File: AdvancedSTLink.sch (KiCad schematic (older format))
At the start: 49 parts, among them J1 USB_C_Receptacle, J2 Conn_02x03_Odd_Even, J3 Conn_01x06, J4 Conn_02x03_Odd_Even, SW1 SW_SPDT, U1 STM32F205RETx, U2 XC6206P332MR, U3 USBLC6-2P6, U4 MP2359, U5 USBLC6-2P6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

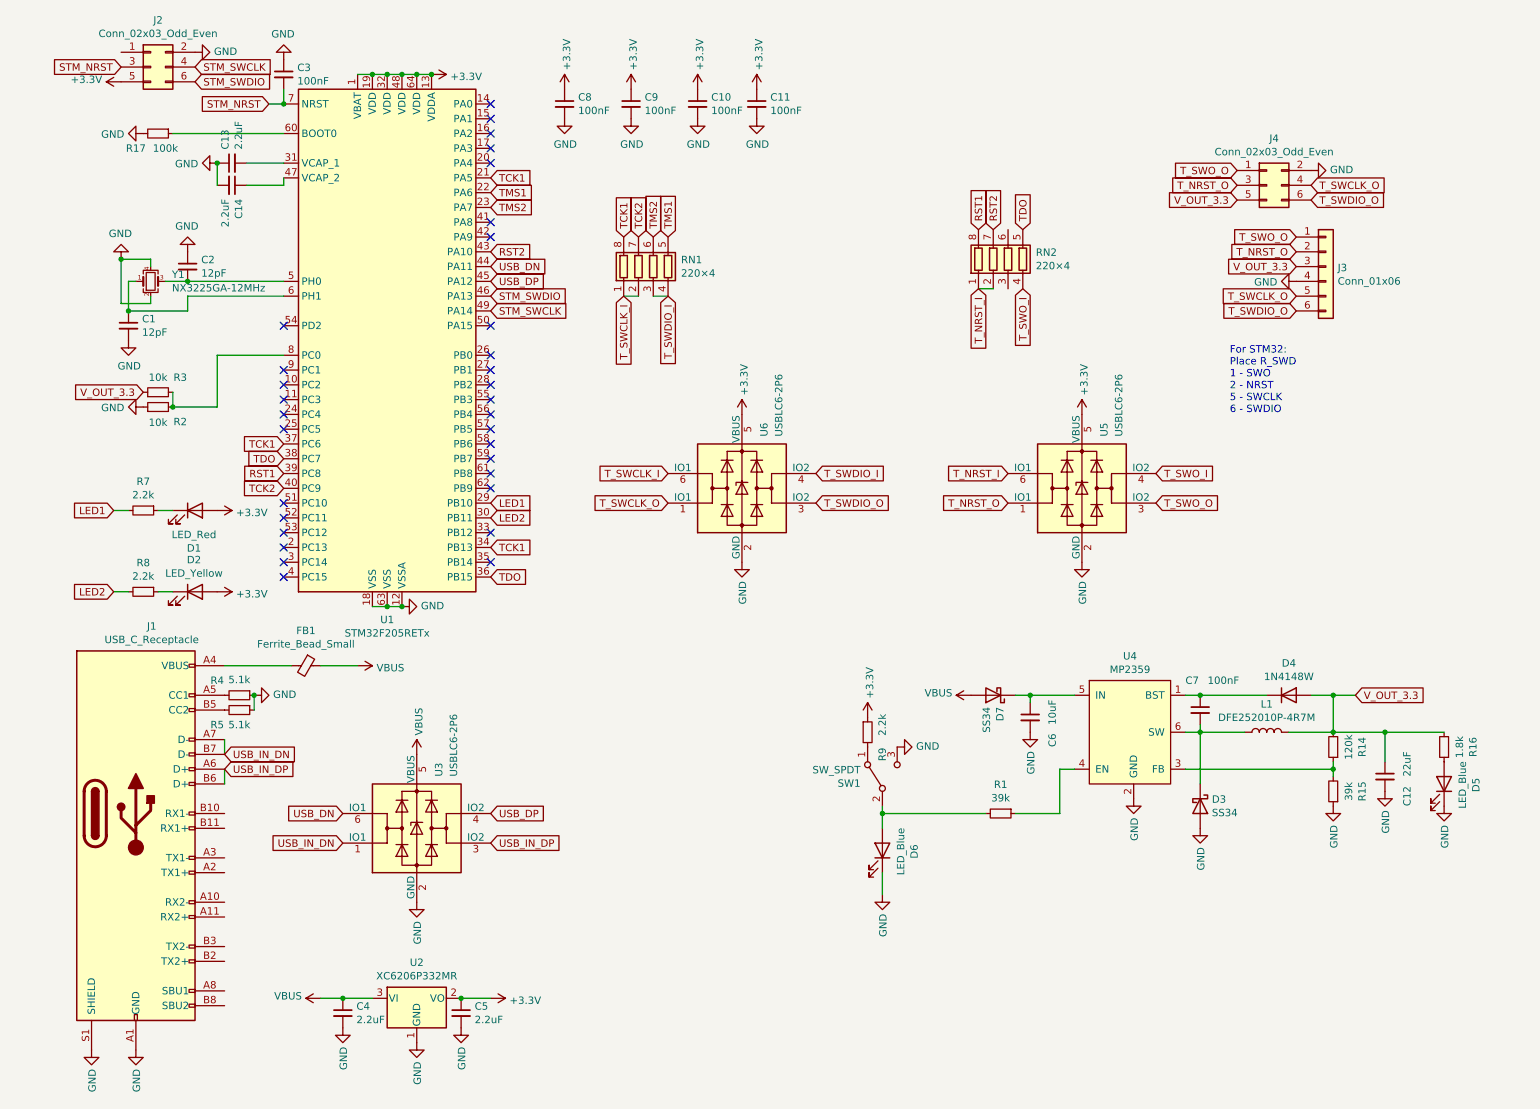
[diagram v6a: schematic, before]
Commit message: Put components.
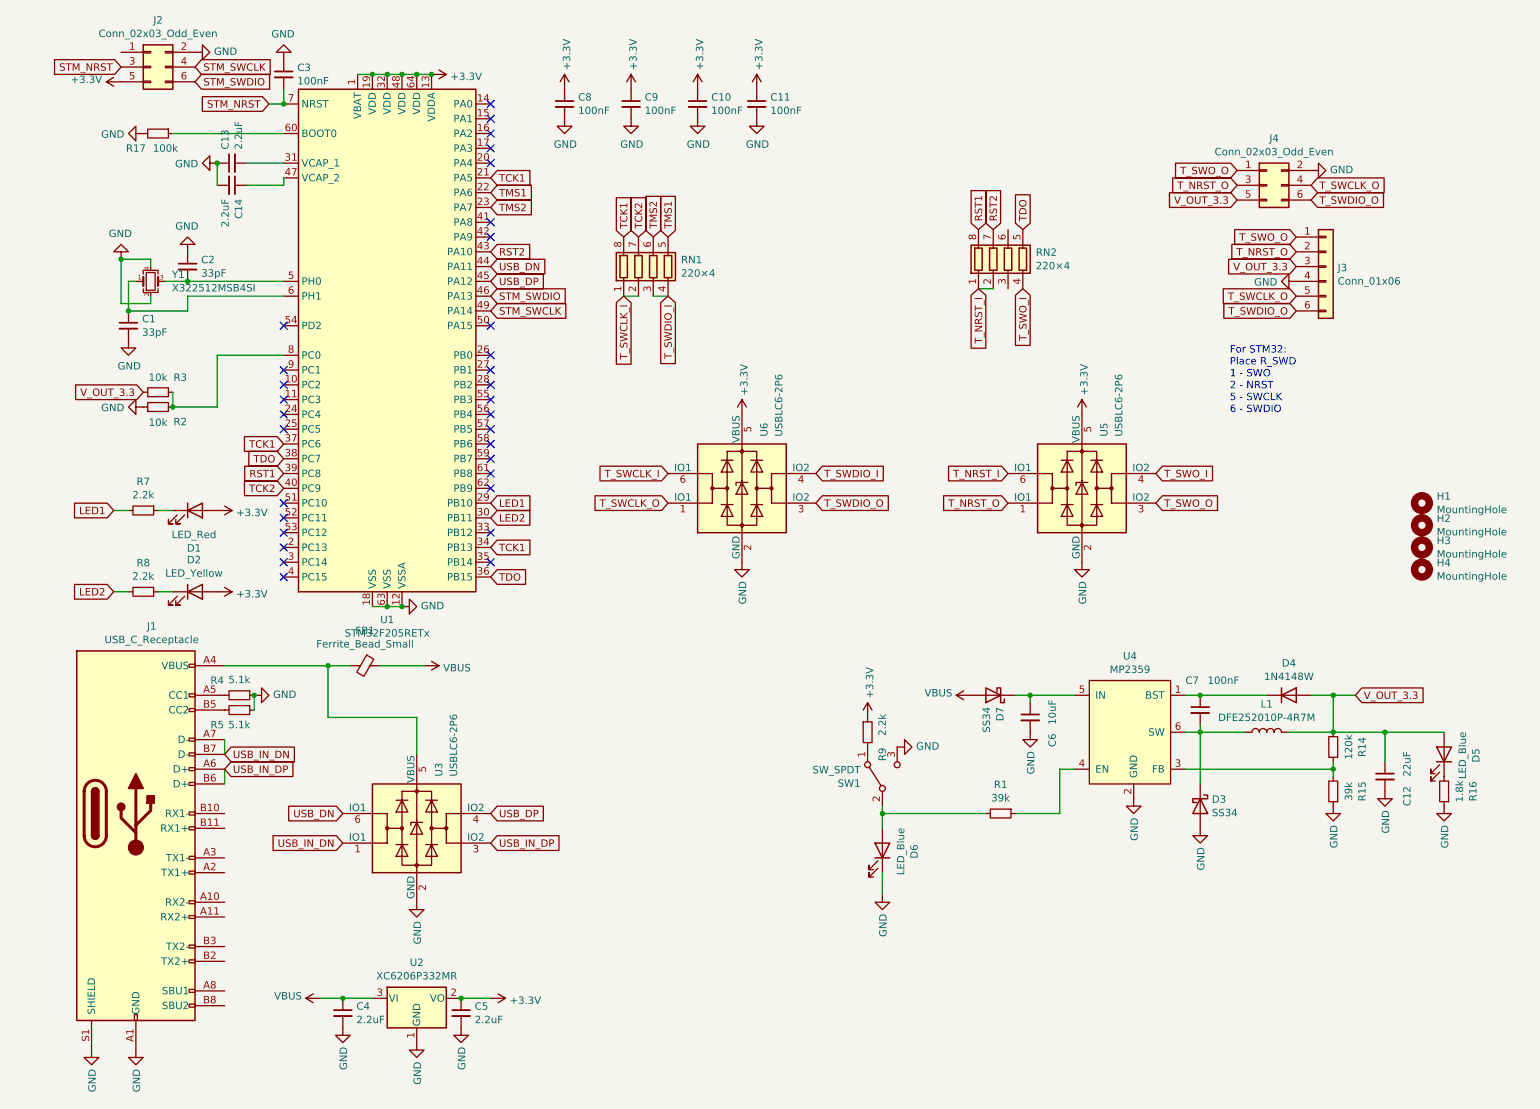
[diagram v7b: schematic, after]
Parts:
- added H1, H2, H3, H4: MountingHole, MountingHole:MountingHole_2.5mm, symbol Mechanical:MountingHole
- C1, C2: value 12pF -> 33pF
- D4: footprint lc:SOD-123 -> lc:SOD-323
- R3: footprint Resistor_SMD:R_0603_1608Metric -> Resistor_SMD:R_0402_1005Metric
- Y1: value NX3225GA-12MHz -> X322512MSB4SI; JLC-ID (none) -> C9002
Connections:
- net GND: now also R16.1; no longer D5.1 (K)
- net VBUS: no longer U3.5 (VBUS)
- net V_OUT_3.3: now also D5.2 (A); no longer R16.2
- net at FB1.2, J1.A4 (VBUS), J1.A9 (VBUS)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: now also U3.5 (VBUS)
- new net: D5.1 (K), R16.2
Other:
- moved on the sheet: D5, FB1, R16
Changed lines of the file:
@@
 P 1050 2600
 F 0 "C1" H 1142 2646 50  0000 L CNN
-F 1 "12pF" H 1142 2555 50  0000 L CNN
+F 1 "33pF" H 1142 2555 50  0000 L CNN
 F 2 "Capacitor_SMD:C_0402_1005Metric" H 1050 2600 50  0001 C CNN
 F 3 "~" H 1050 2600 50  0001 C CNN
@@
 P 1450 2200
 F 0 "C2" H 1542 2246 50  0000 L CNN
-F 1 "12pF" H 1542 2155 50  0000 L CNN
+F 1 "33pF" H 1542 2155 50  0000 L CNN
 F 2 "Capacitor_SMD:C_0402_1005Metric" H 1450 2200 50  0001 C CNN
 F 3 "~" H 1450 2200 50  0001 C CNN
@@
 F 0 "R3" V 1350 2900 50  0000 C CNN
 F 1 "10k" V 1350 3050 50  0000 C CNN
-F 2 "Resistor_SMD:R_0603_1608Metric" H 1250 3050 50  0001 C CNN
+F 2 "Resistor_SMD:R_0402_1005Metric" H 1250 3050 50  0001 C CNN
 F 3 "~" H 1250 3050 50  0001 C CNN
 	1    1250 3050
@@
 L power:VBUS #PWR09
 U 1 1 5E9BBDB8
-P 2600 4900
-F 0 "#PWR09" H 2600 4750 50  0001 C CNN
-F 1 "VBUS" V 2615 5028 50  0000 L CNN
-F 2 "" H 2600 4900 50  0001 C CNN
-F 3 "" H 2600 4900 50  0001 C CNN
-	1    2600 4900
-	0    1    1    0
-$EndComp
-$Comp
-L power:VBUS #PWR018
-U 1 1 5E9BC3AE
-P 3000 5500
-F 0 "#PWR018" H 3000 5350 50  0001 C CNN
-F 1 "VBUS" V 3015 5628 50  0000 L CNN
-F 2 "" H 3000 5500 50  0001 C CNN
-F 3 "" H 3000 5500 50  0001 C CNN
-	1    3000 5500
-	1    0    0    -1
+P 3050 4900
+F 0 "#PWR09" H 3050 4750 50  0001 C CNN
+F 1 "VBUS" V 3065 5028 50  0000 L CNN
+F 2 "" H 3050 4900 50  0001 C CNN
+F 3 "" H 3050 4900 50  0001 C CNN
+	1    3050 4900
+	0    1    1    0
 $EndComp
 $Comp
@@
 F 0 "D4" H 8900 5317 50  0000 C CNN
 F 1 "1N4148W" H 8900 5226 50  0000 C CNN
-F 2 "lc:SOD-123" H 8900 4925 50  0001 C CNN
+F 2 "lc:SOD-323" H 8900 4925 50  0001 C CNN
 F 3 "https://www.vishay.com/docs/85748/1n4148w.pdf" H 8900 5100 50  0001 C CNN
 	1    8900 5100
@@
 L Device:LED D5
 U 1 1 5EA7B230
-P 9950 5700
-F 0 "D5" H 9943 5916 50  0000 C CNN
-F 1 "LED_Blue" H 9943 5825 50  0000 C CNN
-F 2 "LED_SMD:LED_0603_1608Metric_Pad1.05x0.95mm_HandSolder" H 9950 5700 50  0001 C CNN
-F 3 "~" H 9950 5700 50  0001 C CNN
-	1    9950 5700
+P 9950 5500
+F 0 "D5" H 9943 5716 50  0000 C CNN
+F 1 "LED_Blue" H 9943 5625 50  0000 C CNN
+F 2 "LED_SMD:LED_0603_1608Metric_Pad1.05x0.95mm_HandSolder" H 9950 5500 50  0001 C CNN
+F 3 "~" H 9950 5500 50  0001 C CNN
+	1    9950 5500
 	0    1    -1   0
 $EndComp
@@
 L Device:R_Small R16
 U 1 1 5EA7B244
-P 9950 5450
-F 0 "R16" V 9754 5450 50  0000 C CNN
-F 1 "1.8k" V 9845 5450 50  0000 C CNN
-F 2 "Resistor_SMD:R_0402_1005Metric" H 9950 5450 50  0001 C CNN
-F 3 "~" H 9950 5450 50  0001 C CNN
-	1    9950 5450
+P 9950 5750
+F 0 "R16" V 9754 5750 50  0000 C CNN
+F 1 "1.8k" V 9845 5750 50  0000 C CNN
+F 2 "Resistor_SMD:R_0402_1005Metric" H 9950 5750 50  0001 C CNN
+F 3 "~" H 9950 5750 50  0001 C CNN
+	1    9950 5750
 	-1   0    0    1
 $EndComp
@@
 P 1200 2300
 F 0 "Y1" H 1344 2346 50  0000 L CNN
-F 1 "NX3225GA-12MHz" H 1344 2255 50  0000 L CNN
+F 1 "X322512MSB4SI" H 1344 2255 50  0000 L CNN
 F 2 "Crystal:Crystal_SMD_3225-4Pin_3.2x2.5mm" H 1200 2300 50  0001 C CNN
 F 3 "~" H 1200 2300 50  0001 C CNN
+F 4 "C9002 " H 1200 2300 50  0001 C CNN "JLC-ID"
 	1    1200 2300
 	1    0    0    -1
@@
 $EndComp
 Connection ~ 1000 2150
-Wire Wire Line
-	1700 4900 2150 4900
 $Comp
 L Device:Ferrite_Bead_Small FB1
 U 1 1 5EDCF1A8
-P 2250 4900
-F 0 "FB1" V 2013 4900 50  0000 C CNN
-F 1 "Ferrite_Bead_Small" V 2104 4900 50  0000 C CNN
-F 2 "Inductor_SMD:L_0603_1608Metric" V 2180 4900 50  0001 C CNN
-F 3 "~" H 2250 4900 50  0001 C CNN
-	1    2250 4900
-	0    1    1    0
-$EndComp
-Wire Wire Line
-	2350 4900 2600 4900
+P 2650 4900
+F 0 "FB1" V 2413 4900 50  0000 C CNN
+F 1 "Ferrite_Bead_Small" V 2504 4900 50  0000 C CNN
+F 2 "Inductor_SMD:L_0603_1608Metric" V 2580 4900 50  0001 C CNN
+F 3 "~" H 2650 4900 50  0001 C CNN
+	1    2650 4900
+	0    1    1    0
+$EndComp
 Text GLabel 6900 1950 1    50   Input ~ 0
 RST2
@@
 	1    6150 5650
 	0    -1   -1   0
-$EndComp
-$Comp
-L Diode:B230 D7
-U 1 1 5EE1CE14
-P 6900 5100
-F 0 "D7" V 6854 5179 50  0000 L CNN
-F 1 "SS34" V 6945 5179 50  0000 L CNN
-F 2 "lc:SMA(DO-214AC)_S1" H 6900 4925 50  0001 C CNN
-F 3 "http://www.jameco.com/Jameco/Products/ProdDS/1538777.pdf" H 6900 5100 50  0001 C CNN
-	1    6900 5100
-	-1   0    0    1
 $EndComp
 $Comp
@@
 Text GLabel 8550 1550 0    50   Input ~ 0
 T_SWO_O
+$Comp
+L Mechanical:MountingHole H1
+U 1 1 5EF37249
+P 9800 3800
+F 0 "H1" V 9754 3900 50  0000 L CNN
+F 1 "MountingHole" V 9845 3900 50  0000 L CNN
+F 2 "MountingHole:MountingHole_2.5mm" H 9800 3800 50  0001 C CNN
+F 3 "~" H 9800 3800 50  0001 C CNN
+	1    9800 3800
+	0    1    1    0
+$EndComp
+$Comp
+L Mechanical:MountingHole H2
+U 1 1 5EF396E5
+P 9800 3950
+F 0 "H2" V 9754 4050 50  0000 L CNN
+F 1 "MountingHole" V 9845 4050 50  0000 L CNN
+F 2 "MountingHole:MountingHole_2.5mm" H 9800 3950 50  0001 C CNN
+F 3 "~" H 9800 3950 50  0001 C CNN
+	1    9800 3950
+	0    1    1    0
+$EndComp
+$Comp
+L Mechanical:MountingHole H3
+U 1 1 5EF3985B
+P 9800 4100
+F 0 "H3" V 9754 4200 50  0000 L CNN
+F 1 "MountingHole" V 9845 4200 50  0000 L CNN
+F 2 "MountingHole:MountingHole_2.5mm" H 9800 4100 50  0001 C CNN
+F 3 "~" H 9800 4100 50  0001 C CNN
+	1    9800 4100
+	0    1    1    0
+$EndComp
+$Comp
+L Mechanical:MountingHole H4
+U 1 1 5EF39A32
+P 9800 4250
+F 0 "H4" V 9754 4350 50  0000 L CNN
+F 1 "MountingHole" V 9845 4350 50  0000 L CNN
+F 2 "MountingHole:MountingHole_2.5mm" H 9800 4250 50  0001 C CNN
+F 3 "~" H 9800 4250 50  0001 C CNN
+	1    9800 4250
+	0    1    1    0
+$EndComp
+Wire Wire Line
+	2750 4900 3050 4900
+Wire Wire Line
+	1700 4900 2400 4900
+Wire Wire Line
+	2400 4900 2400 5250
+Wire Wire Line
+	2400 5250 3000 5250
+Wire Wire Line
+	3000 5250 3000 5500
+Connection ~ 2400 4900
+Wire Wire Line
+	2400 4900 2550 4900
+$Comp
+L Diode:B230 D7
+U 1 1 5EE1CE14
+P 6900 5100
+F 0 "D7" V 6854 5179 50  0000 L CNN
+F 1 "SS34" V 6945 5179 50  0000 L CNN
+F 2 "lc:SMA(DO-214AC)_S1" H 6900 4925 50  0001 C CNN
+F 3 "http://www.jameco.com/Jameco/Products/ProdDS/1538777.pdf" H 6900 5100 50  0001 C CNN
+	1    6900 5100
+	-1   0    0    1
+$EndComp
 $EndSCHEMATC

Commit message: Layout.
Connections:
- net GND: now also D5.1 (K); no longer R16.1
- net V_OUT_3.3: now also R16.2; no longer D5.2 (A)
- new net: D5.2 (A), R16.1
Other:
- moved on the sheet: D5, R16
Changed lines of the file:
@@
 L Device:LED D5
 U 1 1 5EA7B230
-P 9950 5500
-F 0 "D5" H 9943 5716 50  0000 C CNN
-F 1 "LED_Blue" H 9943 5625 50  0000 C CNN
-F 2 "LED_SMD:LED_0603_1608Metric_Pad1.05x0.95mm_HandSolder" H 9950 5500 50  0001 C CNN
-F 3 "~" H 9950 5500 50  0001 C CNN
-	1    9950 5500
+P 9950 5700
+F 0 "D5" H 9943 5916 50  0000 C CNN
+F 1 "LED_Blue" H 9943 5825 50  0000 C CNN
+F 2 "LED_SMD:LED_0603_1608Metric_Pad1.05x0.95mm_HandSolder" H 9950 5700 50  0001 C CNN
+F 3 "~" H 9950 5700 50  0001 C CNN
+	1    9950 5700
 	0    1    -1   0
 $EndComp
@@
 L Device:R_Small R16
 U 1 1 5EA7B244
-P 9950 5750
-F 0 "R16" V 9754 5750 50  0000 C CNN
-F 1 "1.8k" V 9845 5750 50  0000 C CNN
-F 2 "Resistor_SMD:R_0402_1005Metric" H 9950 5750 50  0001 C CNN
-F 3 "~" H 9950 5750 50  0001 C CNN
-	1    9950 5750
+P 9950 5450
+F 0 "R16" V 9754 5450 50  0000 C CNN
+F 1 "1.8k" V 9845 5450 50  0000 C CNN
+F 2 "Resistor_SMD:R_0402_1005Metric" H 9950 5450 50  0001 C CNN
+F 3 "~" H 9950 5450 50  0001 C CNN
+	1    9950 5450
 	-1   0    0    1
 $EndComp
